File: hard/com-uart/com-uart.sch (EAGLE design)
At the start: 10 parts, among them J1 J0006D21

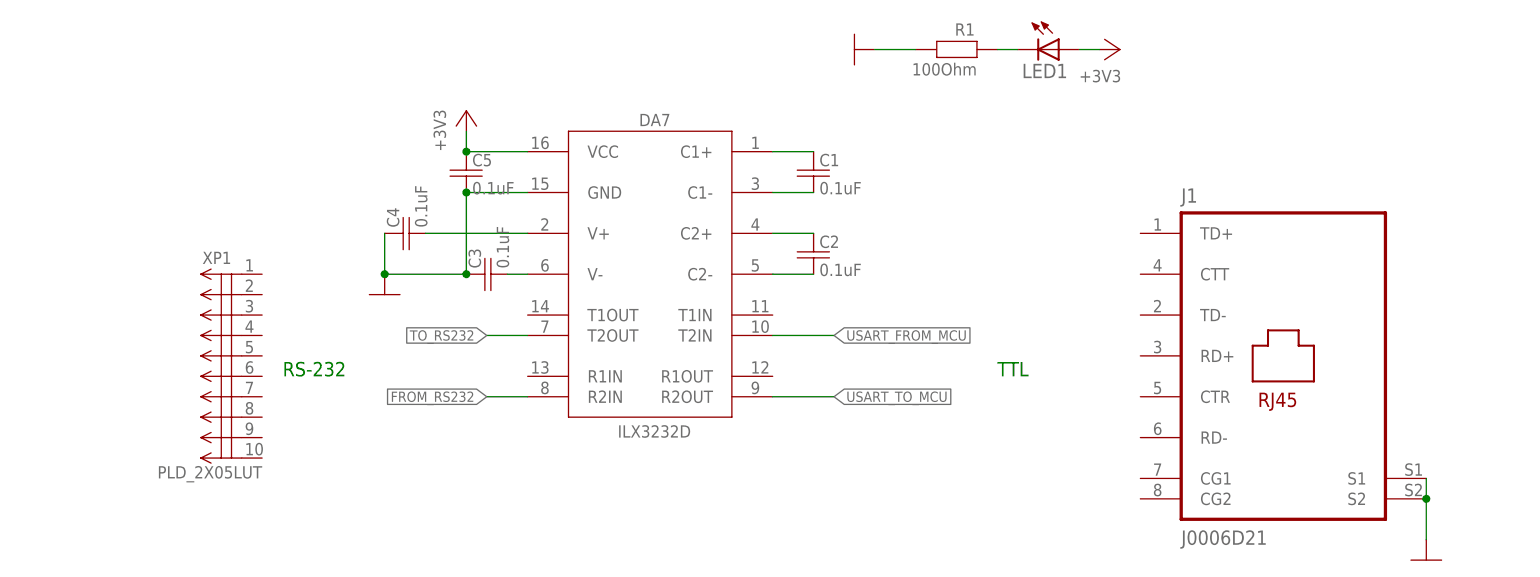
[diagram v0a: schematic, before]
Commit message: almost finished pcb for com-uart
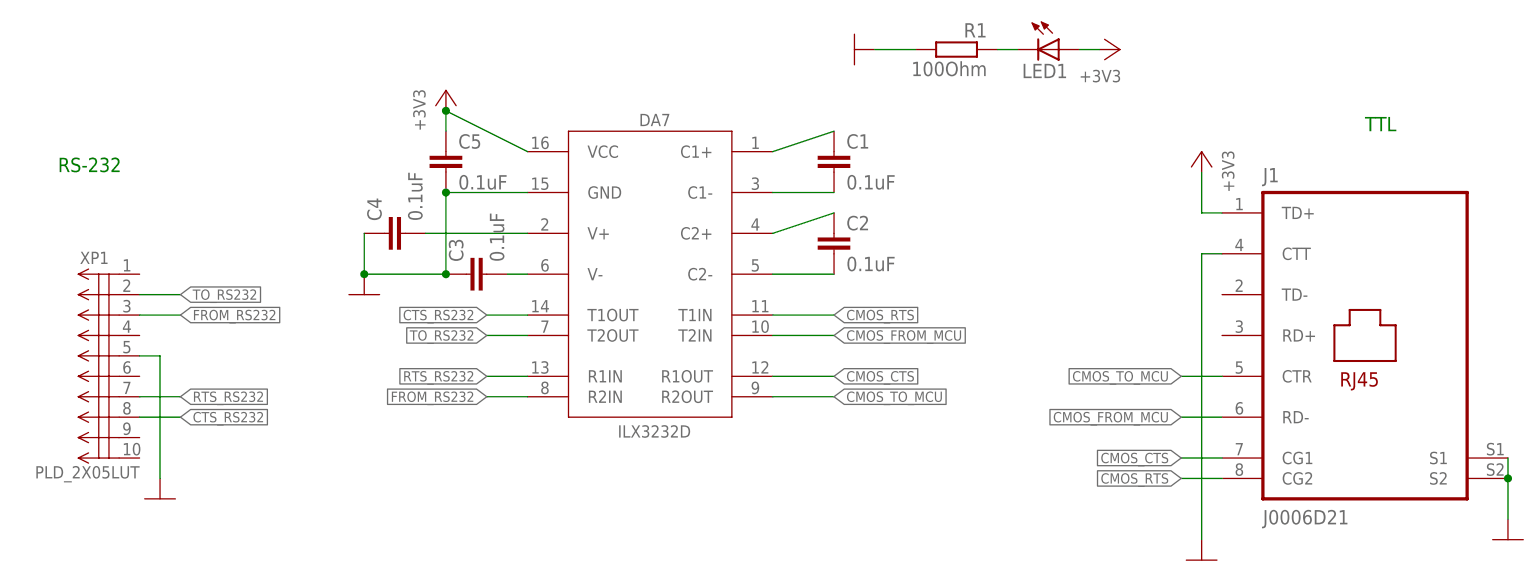
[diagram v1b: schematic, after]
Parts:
- C1, C2, C3, C4, C5: device rcl:C-EUC0805 -> barthess:CAP0805
- R1: device rcl:R-EU_R0805 -> barthess:RESISTOR0805
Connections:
- removed net USART_FROM_MCU: DA7.T2IN
- removed net USART_TO_MCU: DA7.R2OUT
- new net CMOS_CTS: DA7.R1OUT, J1.CG1
- new net CMOS_FROM_MCU: DA7.T2IN, J1.RD-
- new net CMOS_RTS: DA7.T1IN, J1.CG2
- new net CMOS_TO_MCU: DA7.R2OUT, J1.CTR
- new net CTS_RS232: DA7.T1OUT, XP1.8
- new net RTS_RS232: DA7.R1IN, XP1.7
- net +3V3: now also J1.TD+
- net FROM_RS232: now also XP1.3
- net GND: now also J1.CTT, XP1.5
- net TO_RS232: now also XP1.2
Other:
- moved on the sheet: J1, XP1
